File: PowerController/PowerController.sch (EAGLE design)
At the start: 97 parts, among them J11 M10X2, Q1 INFINEON_2N7002_DW, Q2 INFINEON_2N7002_DW, Q3 BS250F, Q4 BS250F, Q5 INFINEON_2N7002_DW, Q6 INFINEON_2N7002_DW, Q7 INFINEON_2N7002_DW, U1 MSP430F5521/5/7/9_PN80, U2 LTV-817, U3 SN74LV74, U4 SN74LV08

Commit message: Removed irrelevant circuits for PC2CAN and Power Controller
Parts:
- removed C11, C12: 0.1uF, rcl:C-USC0603
- removed JP10, JP11, JP13: M023.5MM, SparkFun-Connectors:M023.5MM
- removed JP14, JP7: (no value), SparkFun-Connectors:M04SCREW
- removed JP15: (no value), SparkFun-Connectors:M07
- removed JP6: (no value), SparkFun-Connectors:M05LOCK
- removed JP8: M02LOCK, SparkFun-Connectors:M02LOCK
- removed LED10, LED11, LED8, LED9: (no value), SparkFun-LED:LED0603
- removed Q1, Q6, Q7: INFINEON_2N7002_DW, npol-discrete:INFINEON_2N7002_DW
- removed R13, R27, R28, R33, R34: 0, rcl:R-US_R0603
- removed R23, R24: 10k, rcl:R-US_R0603
- removed R29, R30, R31, R32: 1k, rcl:R-US_R0603
- removed U3: SN74LV74, npol-digital:SN74LV74
- removed U4: SN74LV08, npol-digital:SN74LV08
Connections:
- removed net DRILL_RELAY_1: JP14.4, Q6G$1.DRAIN
- removed net DRILL_RELAY_2: JP14.3, Q6G$2.DRAIN
- removed net DRILL_RELAY_3: JP14.2, Q7G$1.DRAIN
- removed net DRILL_RELAY_4: JP14.1, Q7G$2.DRAIN
- removed net ESTOP_RELAY: JP13.2, Q1G$1.SOURCE, Q1G$2.SOURCE
- removed net N$14: LED9.A, R30.1
- removed net N$20: U31.Q, U41.A
- removed net N$22: U31./Q, U42.B
- removed net N$23: U32.Q, U43.A
- removed net N$25: U32./Q, U44.B
- removed net N$26: R27.1, U31./PRE
- removed net N$27: R28.2, U31./CLR
- removed net N$28: R33.1, U32./PRE
- removed net N$29: R34.2, U32./CLR
- removed net N$33: LED11.A, R32.1
- removed net RC_PWR: JP6.2, JP8.1
- removed net RC_S3: JP6.5, R13.2
- removed net RELAY1_CNTRL: Q6G$1.GATE, R29.2, U41.Y
- removed net RELAY1_LED_A: LED8.A, R29.1
- removed net RELAY2_CNTRL: Q6G$2.GATE, R30.2, U42.Y
- removed net RELAY3_CNTRL: Q7G$1.GATE, R31.2, U43.Y
- removed net RELAY3_LED_A: LED10.A, R31.1
- removed net RELAY4_CNTRL: Q7G$2.GATE, R32.2, U44.Y
- removed net VOC: JP15.7
- net +12V: no longer JP13.1
- net +3V3: no longer C11.1, C12.1, JP15.2, R23.2, R24.2, R27.2, R28.1, R33.2, R34.1, U31.VCC, U41.VCC
- net +5V: no longer JP7.4, JP8.2
- net DRILL_EN: no longer U31.CLK, U32.CLK, U41.B, U42.A, U43.B, U44.A
- net DRILL_ISENSE_/FAULT: no longer JP15.5
- net DRILL_ISENSE_FAULT_EN: no longer JP15.6
- net DRILL_ISENSE_VIOUT: no longer JP15.3
- net DRILL_ISENSE_VZCR: no longer JP15.4
- net DRILL_S1: no longer U31.D
- net DRILL_S2: no longer U32.D
- net ESTOP_LOCAL: no longer Q1G$1.GATE, Q1G$2.GATE, R13.1
- net GND: no longer C11.2, C12.2, JP10.1, JP11.1, JP15.1, JP6.1, LED10.C, LED11.C, LED8.C, LED9.C, Q1G$1.DRAIN, Q1G$2.DRAIN, Q6G$1.SOURCE, Q6G$2.SOURCE, Q7G$1.SOURCE, Q7G$2.SOURCE, U31.GND, U41.GND
- net LOWER_SWITCH: no longer JP11.2, R24.1
- net RC_S1: no longer JP6.3
- net RC_S2: no longer JP6.4
- net STEPPER_DIR: no longer JP7.2
- net STEPPER_EN: no longer JP7.3
- net STEPPER_STEP: no longer JP7.1
- net UPPER_SWITCH: no longer JP10.2, R23.1
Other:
- note added: "TODO: ESTOP Driver/Relay"
- note added: "TODO: Xbee"
- note removed: "ACS709 Current Sensor"
- note removed: "ESTOP Relay Output shared with Drill and Stepper ESTOP relays"
- note removed: "Roboclaw"
- note removed: "Stepper driver"
- note removed: "VOC Unused"

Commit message: Power Controller ready for fab
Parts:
- removed JP12: M02LOCK, SparkFun-Connectors:M02LOCK
- removed JP9: M02POLAR_LOCK, SparkFun-Connectors:M02POLAR_LOCK
- removed U2: LTV-817, npol-digital:LTV-817
- added JP6: (no value), SparkFun-Connectors:M03LOCK
- added JP7: M02POLAR_LOCK, SparkFun-Connectors:M02POLAR_LOCK
- added LED10, LED8, LED9: (no value), SparkFun-LED:LED0603
- added Q1: INFINEON_2N7002_DW, npol-discrete:INFINEON_2N7002_DW
- added R13, R23: 10k, rcl:R-US_R0603
- added R24: 470, rcl:R-US_R0603
- added R27: 330, rcl:R-US_R0603
- added XB1: XBEE, microbuilder:XBEE
- H3: value MOUNT-PAD-ROUND3.2 -> MOUNT-HOLE3.2; device holes:MOUNT-PAD-ROUND3.2 -> holes:MOUNT-HOLE3.2
- JP1: device SparkFun-Connectors:M03X22X3_SILK_SM -> SparkFun-Connectors:M05PTH
- JP2: value M02LOCK -> (none); device SparkFun-Connectors:M02LOCK -> SparkFun-Connectors:M03X22X3_SILK_SM
- JP3: value ONSHORE_OST302-S141 -> M02LOCK; device npol-connectors:ONSHORE_OST302-S141 -> SparkFun-Connectors:M02LOCK
- JP4: value FTDI_DEVICE -> ONSHORE_OST302-S141; device SparkFun-Connectors:FTDI_DEVICE -> npol-connectors:ONSHORE_OST302-S141
- JP5: value (none) -> FTDI_DEVICE; device SparkFun-Connectors:M03LOCK -> SparkFun-Connectors:FTDI_DEVICE
- Q2: value INFINEON_2N7002_DW -> BS250F; device npol-discrete:INFINEON_2N7002_DW -> SparkFun-DiscreteSemi:MOSFET-PCHANNELSMD
- Q4: value BS250F -> INFINEON_2N7002_DW; device SparkFun-DiscreteSemi:MOSFET-PCHANNELSMD -> npol-discrete:INFINEON_2N7002_DW
- R17, R20: value 10k -> 100k
- R19, R21: value 100k -> 10k
- R25: value 620 -> 330
- R26: value 10k -> 470
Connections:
- removed net DRILL_EN: U1.P7.6/TB0.4
- removed net DRILL_ISENSE_/FAULT: U1.P1.3/TA0.2
- removed net DRILL_ISENSE_FAULT_EN: U1.P6.0/CB0/A0
- removed net DRILL_ISENSE_VIOUT: U1.P6.2/CB2/A2
- removed net DRILL_ISENSE_VZCR: U1.P6.1/CB1/A1
- removed net DRILL_S1: U1.P7.5/TB0.3
- removed net DRILL_S2: U1.P7.4/TB0.2
- removed net ESTOP+: JP9.1, R25.2
- removed net ESTOP-: JP9.2, U2.2
- removed net ESTOP_LOCAL: JP12.1, Q5G$1.DRAIN, R26.2, U1.P1.4/TA0.3
- removed net ESTOP_LOCAL_INV: Q5G$1.GATE, U2.4
- removed net LOWER_SWITCH: U1.P2.0/TA1.1
- removed net RC_RXD: R14.2, SJ3.3, SJ4.1, U1.P4.5/PM_UCA1RXD/PM_UCA1SOMI
- removed net RC_S1: SJ3.2
- removed net RC_S2: SJ4.2
- removed net RC_TXD: R15.2, SJ3.1, SJ4.3, U1.P4.4/PM_UCA1TXD/PM_UCA1SIMO
- removed net STEPPER_DIR: U1.P7.1/CB9/A13
- removed net STEPPER_EN: U1.P7.2/CB10/A14
- removed net STEPPER_STEP: U1.P1.2/TA0.1
- removed net UPPER_SWITCH: U1.P2.1/TA1.2
- new net ESTOP_INV: LED8.C, Q4G$1.DRAIN, Q4G$2.GATE, R23.2, U1.P1.1/TA0.0
- new net ESTOP_OUT: JP7.1, Q4G$1.GATE, Q5G$1.DRAIN, R25.2
- new net ESTOP_PULLDOWN: Q5G$1.GATE, Q5G$2.GATE, R22.1, U1.P1.2/TA0.1
- new net N$14: LED10.C, R27.1
- new net N$15: LED8.A, R24.2
- new net N$16: Q4G$2.DRAIN, R26.2
- new net N$17: LED9.C, R26.1
- new net NU_P3.7: JP1.5, U1.P3.7/TB0OUTH/SVMOUT
- new net NU_P4.0: JP1.4, U1.P4.0/PM_UCB1STE/PM_UCA1CLK
- new net NU_P4.1: JP1.3, U1.P4.1/PM_UCB1SIMO/PM_UCB1SDA
- new net NU_P4.2: JP1.2, U1.P4.2/PM_UCB1SOMI/PM_UCB1SCL
- new net NU_P4.3: JP1.1, U1.P4.3/PM_UCB1CLK/PM_UCA1STE
- new net XBEE_DIN: SJ3.2, XB1.DIN/!CONFIG
- new net XBEE_DOUT: SJ4.2, XB1.DOUT
- new net XBEE_RXD: R13.2, SJ3.3, SJ4.1, U1.P4.5/PM_UCA1RXD/PM_UCA1SOMI
- new net XBEE_TXD: R14.2, SJ3.1, SJ4.3, U1.P4.4/PM_UCA1TXD/PM_UCA1SIMO
- net +12V: now also Q3.S, R19.2, R25.1; no longer Q4.S, R20.2
- net +3V3: now also JP3.1, JP6.2, LED10.A, LED9.A, R15.2, R23.1, R24.1, XB1.VCC; no longer JP2.1, JP5.2, R16.2, R26.1
- net +5V: now also Q2.S, R16.2; no longer Q3.S, R17.2
- net 12VSENSE: now also R20.1, R21.2; no longer R21.1, R22.2
- net 5VSENSE: now also R17.1, R18.2; no longer R18.1, R19.2
- net GND: now also JP2.2, JP4.9, JP5.GND, JP7.2, Q1G$1.SOURCE, Q1G$2.SOURCE, Q4G$1.SOURCE, Q4G$2.SOURCE, Q5G$2.SOURCE, R13.1, R18.1, R21.1, R22.2, XB1.GND; no longer H3.MOUNT, JP1.2, JP12.2, JP3.9, JP4.GND, Q2G$1.SOURCE, Q2G$2.SOURCE, R15.1, R19.1, R22.1, U2.3
- net N$1: now also JP3.2, JP5.VCC; no longer JP2.2, JP4.VCC
- net N$10: now also Q1G$1.DRAIN, Q2.G, R16.1; no longer Q2G$1.DRAIN, Q3.G, R17.1
- net N$11: now also Q3.D, R20.2; no longer Q4.D, R21.2
- net N$12: now also Q1G$1.GATE, Q1G$2.GATE, R15.1; no longer Q2G$1.GATE, Q2G$2.GATE, R16.1
- net N$13: now also Q5G$2.DRAIN, R27.2; no longer R25.1, U2.1
- net N$9: now also Q2.D, R17.2; no longer Q3.D, R18.2
- net NU_P6.3: now also JP2.5; no longer JP1.5
- net NU_P6.4: now also JP2.6; no longer JP1.6
- net NU_P6.5: now also JP2.3; no longer JP1.3
- net NU_P6.6: now also JP2.4; no longer JP1.4
- net NU_P6.7: now also JP2.1; no longer JP1.1
- net RXI: now also JP5.RXI; no longer JP4.RXI
- net SBWTCK: now also JP4.7; no longer JP3.7
- net SBWTDIO: now also JP4.1; no longer JP3.1
- net TXO: now also JP5.TXO; no longer JP4.TXO
- net VCC_TARGET: now also JP4.4, JP6.1; no longer JP3.4, JP5.1
- net VCC_TOOL: now also JP4.2, JP6.3; no longer JP3.2, JP5.3
- net VTAP_EN: now also Q1G$2.DRAIN, Q3.G, R19.1; no longer Q2G$2.DRAIN, Q4.G, R20.1
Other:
- note removed: "Limit switches"
- note removed: "TODO: ESTOP Driver/Relay"
- note removed: "TODO: Xbee"
- moved on the sheet: Q3, R14, R15, R16, R17, R18, R19, R20, R21, R22, R25, R26

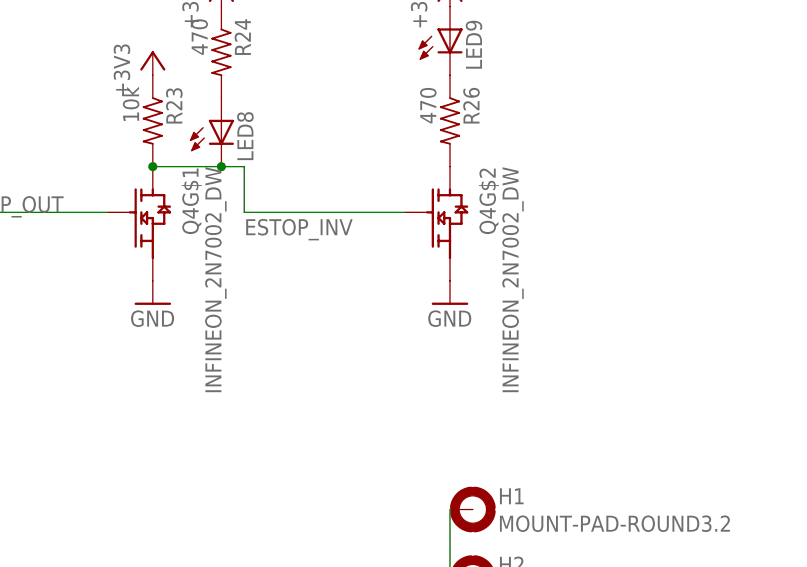
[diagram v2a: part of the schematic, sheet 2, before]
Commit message: Power Controller, Elim-Mobility Controller, and PC2CAN sent to FAB
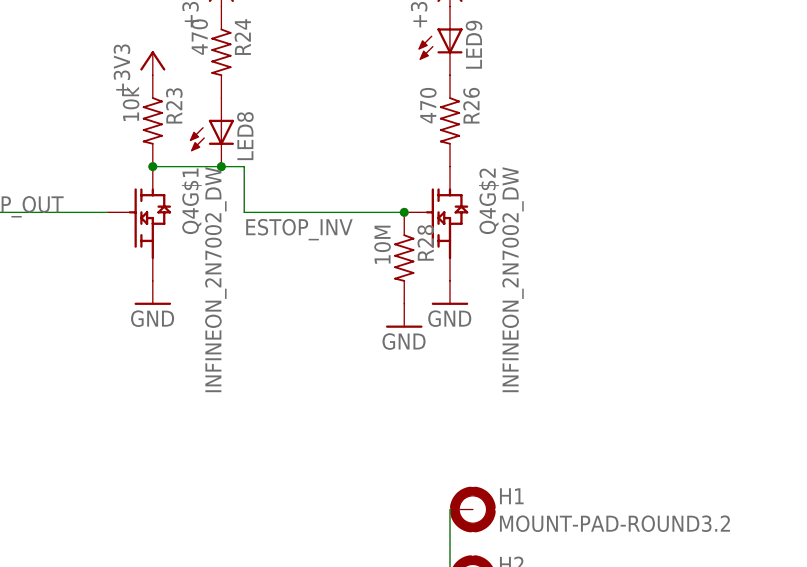
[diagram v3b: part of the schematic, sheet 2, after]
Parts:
- added R28: 10M, rcl:R-US_R0603
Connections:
- net ESTOP_INV: now also R28.1
- net GND: now also R28.2
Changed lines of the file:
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@@
 <part name="R22" library="rcl" deviceset="R-US_" device="R0603" value="10k"/>
 <part name="GND32" library="supply1" deviceset="GND" device=""/>
+<part name="R28" library="rcl" deviceset="R-US_" device="R0603" value="10M"/>
+<part name="GND39" library="supply1" deviceset="GND" device=""/>
 </parts>
 <sheets>
@@
 <instance part="R22" gate="G$1" x="200.66" y="175.26" rot="R270"/>
 <instance part="GND32" gate="1" x="200.66" y="167.64"/>
+<instance part="R28" gate="G$1" x="231.14" y="114.3" rot="R270"/>
+<instance part="GND39" gate="1" x="231.14" y="106.68"/>
 </instances>
 <busses>
@@
 <pinref part="R22" gate="G$1" pin="2"/>
 <pinref part="GND32" gate="1" pin="GND"/>
+</segment>
+<segment>
+<pinref part="R28" gate="G$1" pin="2"/>
+<pinref part="GND39" gate="1" pin="GND"/>
 </segment>
 </net>
@@
 <junction x="210.82" y="124.46"/>
 <label x="213.36" y="116.84" size="1.778" layer="95"/>
-</segment>
-</net>
+<pinref part="R28" gate="G$1" pin="1"/>
+<junction x="231.14" y="119.38"/>
+</segment>
+</net>
